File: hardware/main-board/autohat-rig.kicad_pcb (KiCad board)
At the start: 2 copper layers, 75.4 x 114 mm, 92 parts, among them J1 USDCARD, P1 USB HUB IN, P10 BARREL_JACK, P2 USB MUX 2, P3 USB MUX 1, P4 CONN_01X06, P5 BARREL_JACK, P6 IDC_02X04, P7 IDC_02X04, P8 PWR IN, P9 PWR OUT, Q1 IRF7606PBF, Q2 IRF7606PBF, Q3 IRF7606PBF, Q4 IRF7606PBF, Q5 2N7002, Q6 2N7002, Q7 IRF7606PBF, Q8 IRF7606PBF, U1 TS3USB30EDGSR, U2 FT245RL, U3 TUSB4041IPAPR, U4 74AHC1G14, U5 TLV73333, U6 TLV73311, U7 74AHC1G14, U8 TS3A27518E, Y1 24MHz

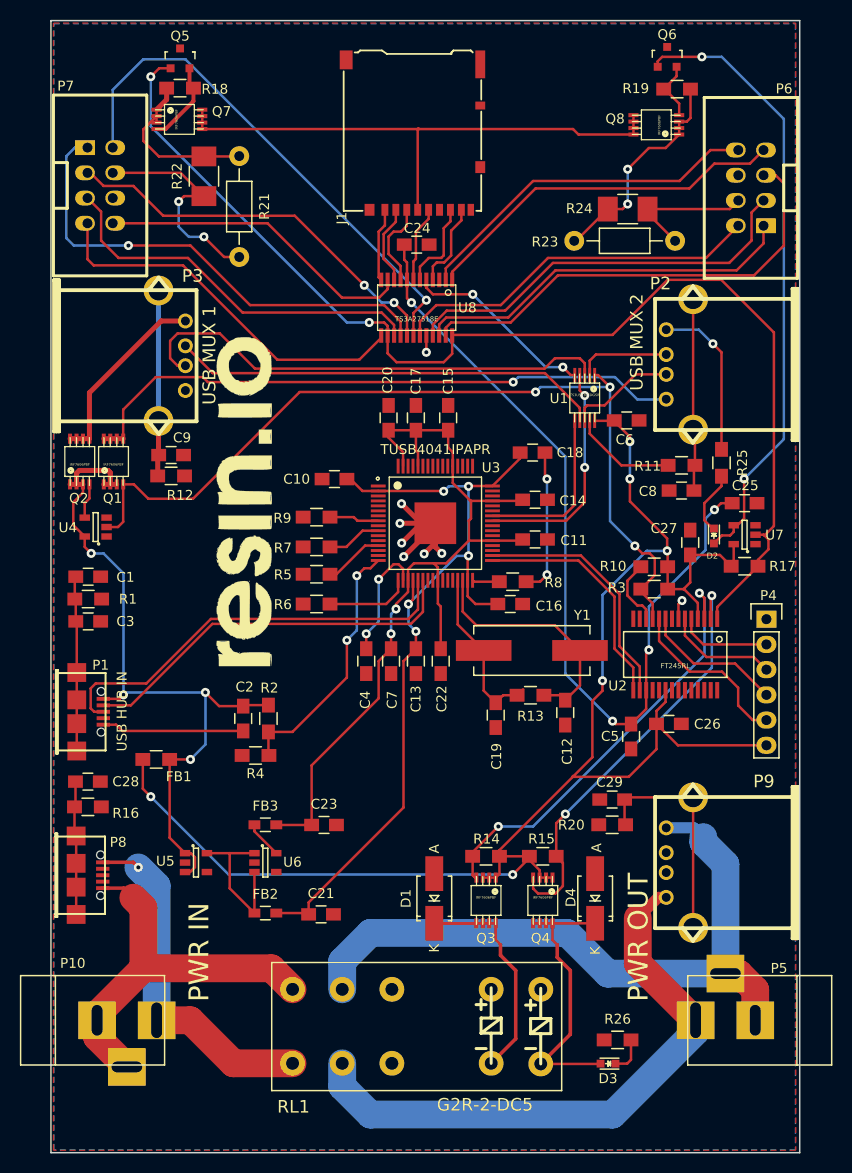
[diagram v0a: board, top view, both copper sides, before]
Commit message: Add mounting holes and labels
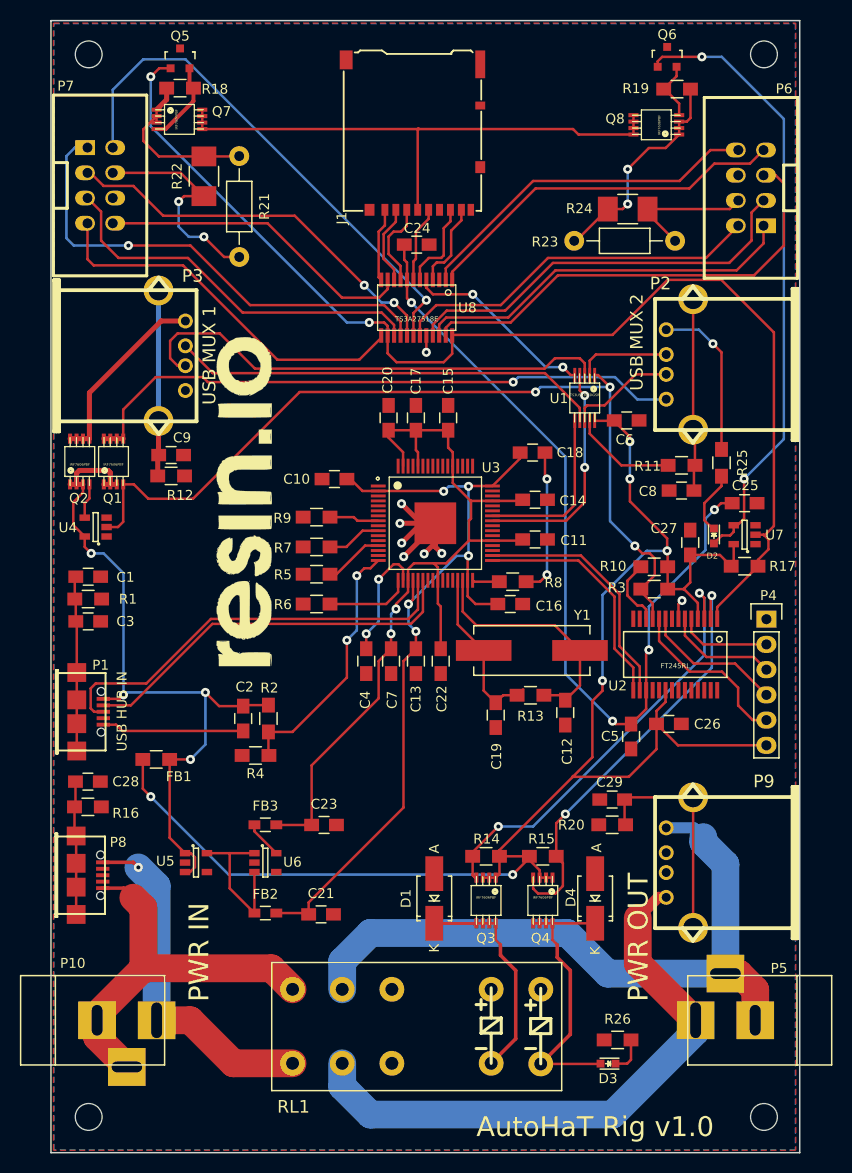
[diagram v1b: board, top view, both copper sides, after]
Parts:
- added REF**: MountingHole_2.7mm_M2.5, Mounting_Holes:MountingHole_2.7mm_M2.5, F.Cu at (122.0, 37.0)
- added REF**: MountingHole_2.7mm_M2.5, Mounting_Holes:MountingHole_2.7mm_M2.5, F.Cu at (190.0, 37.0)
- added REF**: MountingHole_2.7mm_M2.5, Mounting_Holes:MountingHole_2.7mm_M2.5, F.Cu at (122.0, 144.0)
- added REF**: MountingHole_2.7mm_M2.5, Mounting_Holes:MountingHole_2.7mm_M2.5, F.Cu at (190.0, 144.0)
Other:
- board text added: "AutoHaT Rig v1.0"
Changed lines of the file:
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@@
     (area 118.124519 33.525479 193.674521 147.675481)
     (thickness 1.6)
-    (drawings 7)
+    (drawings 9)
     (tracks 829)
     (zones 0)
-    (modules 92)
+    (modules 96)
     (nets 113)
   )
   (page A4)
   (title_block
-    (title sd-mux)
-    (date 2016-02-26)
-    (rev 2)
-    (company SRPOL)
-    (comment 1 "Author: Adam Malinowski <a.malinowsk2@partner.samsung.com>")
+    (title autohat-rig)
+    (date 2016-12-12)
+    (rev 1.0)
+    (company Resin.io)
+    (comment 1 "Author: Adam Malinowski <a.malinowsk2@partner.samsung.com> \\n        Tomás Villaseca <tomas@resin.io>")
     (comment 2 "Copyright (c) 2016 Samsung Electronics Co., Ltd All Rights Reserved")
   )
@@
     (zone_45_only yes)
     (trace_min 0.254)
-    (segment_width 0.2)
+    (segment_width 1)
     (edge_width 0.15)
     (via_size 0.91)
@@
     (pad_to_mask_clearance 0.2)
     (aux_axis_origin 118.19952 147.60048)
-    (visible_elements FFFEEF7F)
+    (visible_elements FFFEFF7F)
     (pcbplotparams
       (layerselection 0x010f0_80000001)
@@
     (add_net VDD)
   )
+  (module Mounting_Holes:MountingHole_2.7mm_M2.5 (layer Front)
+    (at 122 37)
+    (descr "Mounting Hole 2.7mm, no annular, M2.5")
+    (tags "mounting hole 2.7mm no annular m2.5")
+    (fp_text reference REF** (at 0 -3.7) (layer F.SilkS) hide
+      (effects (font (size 1 1) (thickness 0.15)))
+    )
+    (fp_text value MountingHole_2.7mm_M2.5 (at 0 3.7) (layer F.Fab)
+      (effects (font (size 1 1) (thickness 0.15)))
+    )
+    (fp_circle (center 0 0) (end 2.7 0) (layer Cmts.User) (width 0.15))
+    (fp_circle (center 0 0) (end 2.95 0) (layer F.CrtYd) (width 0.05))
+    (pad 1 np_thru_hole circle (at 0 0) (size 2.7 2.7) (drill 2.7) (layers *.Cu *.Mask))
+  )
+  (module Mounting_Holes:MountingHole_2.7mm_M2.5 (layer Front)
+    (at 190 37)
+    (descr "Mounting Hole 2.7mm, no annular, M2.5")
+    (tags "mounting hole 2.7mm no annular m2.5")
+    (fp_text reference REF** (at 0 -3.7) (layer F.SilkS) hide
+      (effects (font (size 1 1) (thickness 0.15)))
+    )
+    (fp_text value MountingHole_2.7mm_M2.5 (at 0 3.7) (layer F.Fab)
+      (effects (font (size 1 1) (thickness 0.15)))
+    )
+    (fp_circle (center 0 0) (end 2.7 0) (layer Cmts.User) (width 0.15))
+    (fp_circle (center 0 0) (end 2.95 0) (layer F.CrtYd) (width 0.05))
+    (pad 1 np_thru_hole circle (at 0 0) (size 2.7 2.7) (drill 2.7) (layers *.Cu *.Mask))
+  )
+  (module Mounting_Holes:MountingHole_2.7mm_M2.5 (layer Front)
+    (at 122 144)
+    (descr "Mounting Hole 2.7mm, no annular, M2.5")
+    (tags "mounting hole 2.7mm no annular m2.5")
+    (fp_text reference REF** (at 0 -3.7) (layer F.SilkS) hide
+      (effects (font (size 1 1) (thickness 0.15)))
+    )
+    (fp_text value MountingHole_2.7mm_M2.5 (at 0 3.7) (layer F.Fab)
+      (effects (font (size 1 1) (thickness 0.15)))
+    )
+    (fp_circle (center 0 0) (end 2.7 0) (layer Cmts.User) (width 0.15))
+    (fp_circle (center 0 0) (end 2.95 0) (layer F.CrtYd) (width 0.05))
+    (pad 1 np_thru_hole circle (at 0 0) (size 2.7 2.7) (drill 2.7) (layers *.Cu *.Mask))
+  )
   (module TO_SOT_Packages_SMD:SOT-23-5 (layer Front)
     (at 188.04952 85.37048 180)
@@
       (effects (font (thickness 0.3048)))
     )
-    (fp_text value G2R-2-DC5 (at -6.87008 -7.87292 180) (layer F.SilkS)
+    (fp_text value G2R-2-DC5 (at -6.87008 -7.87292 180) (layer F.SilkS) hide
       (effects (font (thickness 0.3048)))
     )
@@
       (effects (font (size 1 1) (thickness 0.15)))
     )
-    (fp_text value TUSB4041IPAPR (at 0.01168 -7.43128) (layer F.SilkS)
+    (fp_text value TUSB4041IPAPR (at 0.01168 -7.43128) (layer F.SilkS) hide
       (effects (font (size 1 1) (thickness 0.05)))
     )
@@
       (xy 12.361334 0.889)) (layer F.SilkS) (width 0.01))
   )
+  (module Mounting_Holes:MountingHole_2.7mm_M2.5 (layer Front)
+    (at 190 144)
+    (descr "Mounting Hole 2.7mm, no annular, M2.5")
+    (tags "mounting hole 2.7mm no annular m2.5")
+    (fp_text reference REF** (at 0 -3.7) (layer F.SilkS) hide
+      (effects (font (size 1 1) (thickness 0.15)))
+    )
+    (fp_text value MountingHole_2.7mm_M2.5 (at 0 3.7) (layer F.Fab)
+      (effects (font (size 1 1) (thickness 0.15)))
+    )
+    (fp_circle (center 0 0) (end 2.7 0) (layer Cmts.User) (width 0.15))
+    (fp_circle (center 0 0) (end 2.95 0) (layer F.CrtYd) (width 0.05))
+    (pad 1 np_thru_hole circle (at 0 0) (size 2.7 2.7) (drill 2.7) (layers *.Cu *.Mask))
+  )
+  (gr_line (start 181 41) (end 151 41) (angle 90) (layer B.SilkS) (width 10))
+  (target plus (at 145.75 144.75) (size 5) (width 0.15) (layer Edge.Cuts))
+  (gr_text "AutoHaT Rig v1.0" (at 173 145) (layer F.SilkS)
+    (effects (font (size 2 2) (thickness 0.5)))
+  )
   (dimension 75.3 (width 0.3) (layer Dwgs.User)
     (gr_text "75.300 mm" (at 155.74952 153.85048) (layer Dwgs.User)
@@
     (arrow2b (pts (xy 112.79952 33.60048) (xy 113.385941 34.726984)))
   )
-  (target plus (at 145.75 144.75) (size 5) (width 0.15) (layer Edge.Cuts))
   (gr_line (start 193.59952 147.60048) (end 118.19952 147.60048) (angle 90) (layer Edge.Cuts) (width 0.15))
   (gr_line (start 193.59952 33.60048) (end 193.59952 147.60048) (angle 90) (layer Edge.Cuts) (width 0.15))

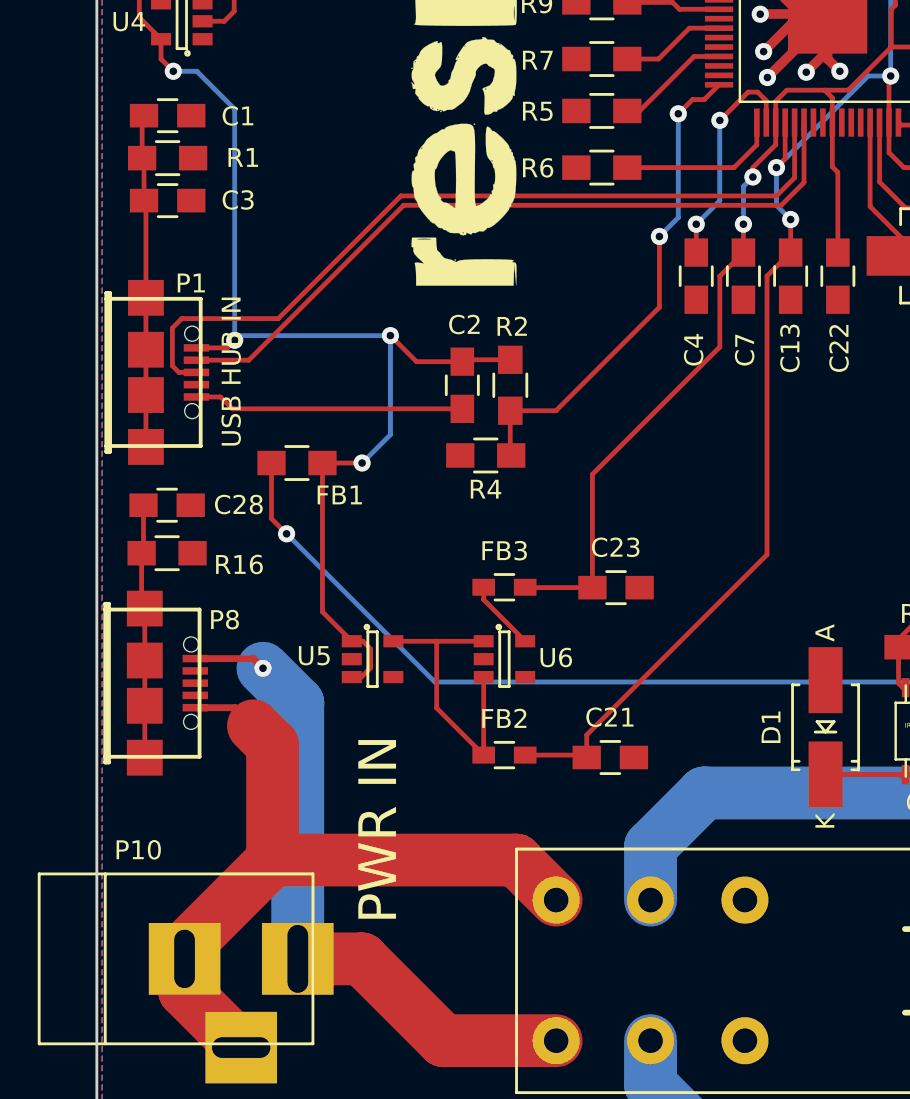
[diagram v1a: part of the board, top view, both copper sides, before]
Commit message: Change micro USB socket to through-hole
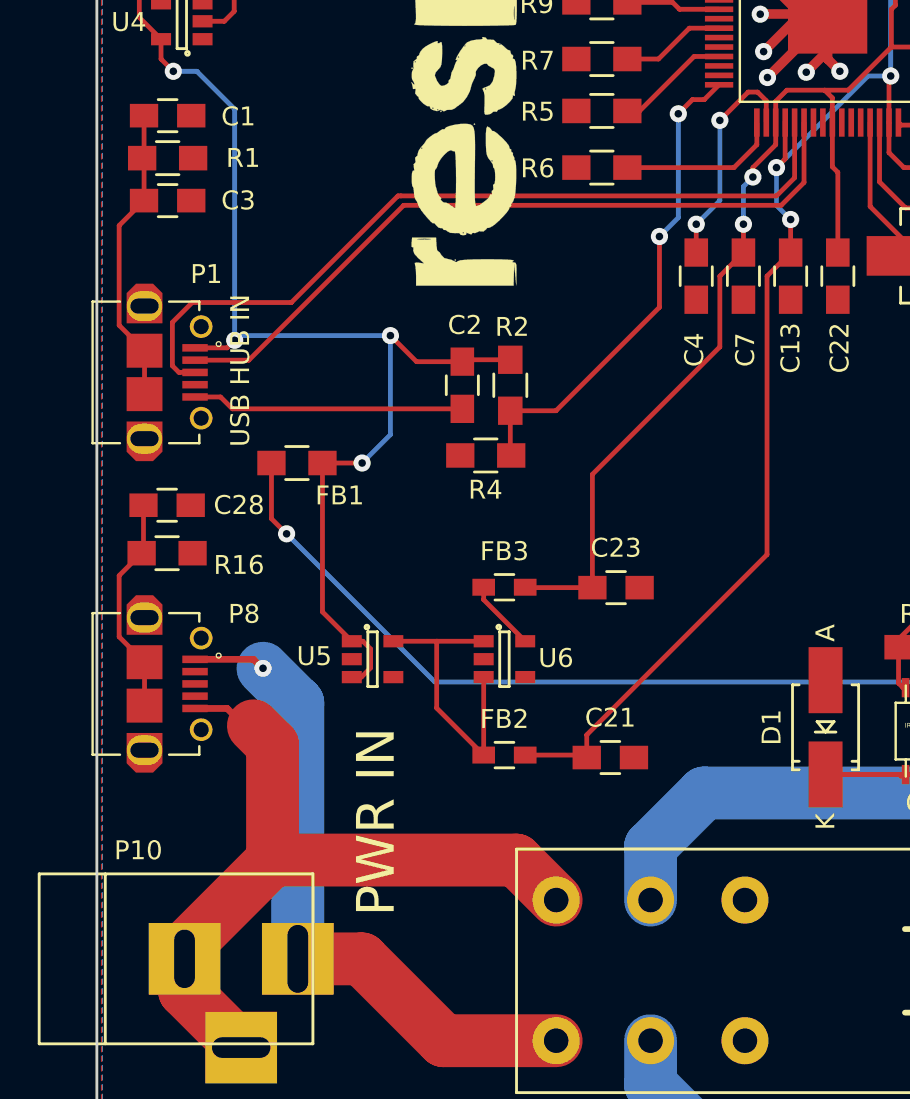
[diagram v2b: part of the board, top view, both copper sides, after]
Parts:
- P1, P8: footprint footprints:conn_usb_B_micro -> footprints:TO_microUSB
- RL1: value G2R-2-DC5 -> G2RK-2-DC5
- moved P8 2.66 mm to (123.4, 119.7)
- moved P1 2.60 mm to (123.4, 103.2)
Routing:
- net Net-(C1-Pad1): track 17.7 -> 15.9 mm
- net Net-(C28-Pad1): track 13.5 -> 11.7 mm

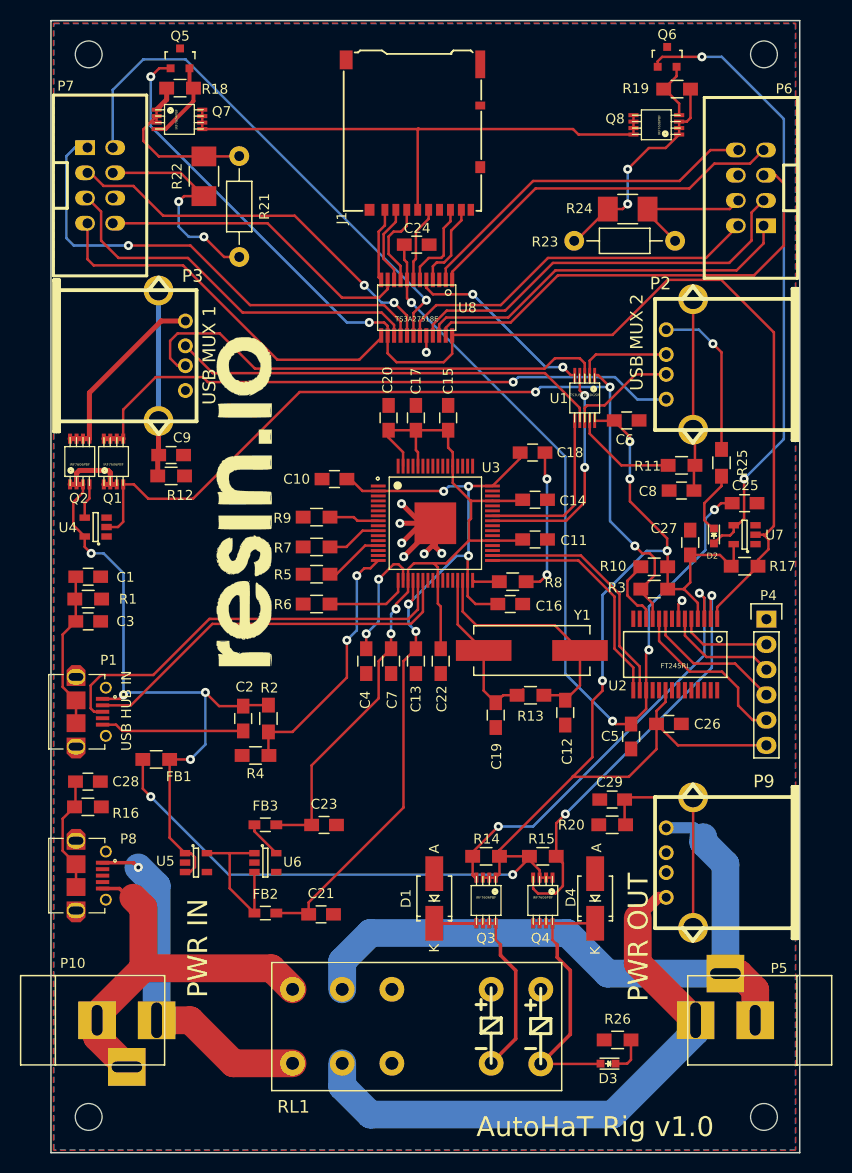
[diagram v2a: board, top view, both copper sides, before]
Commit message: Fix current leakage
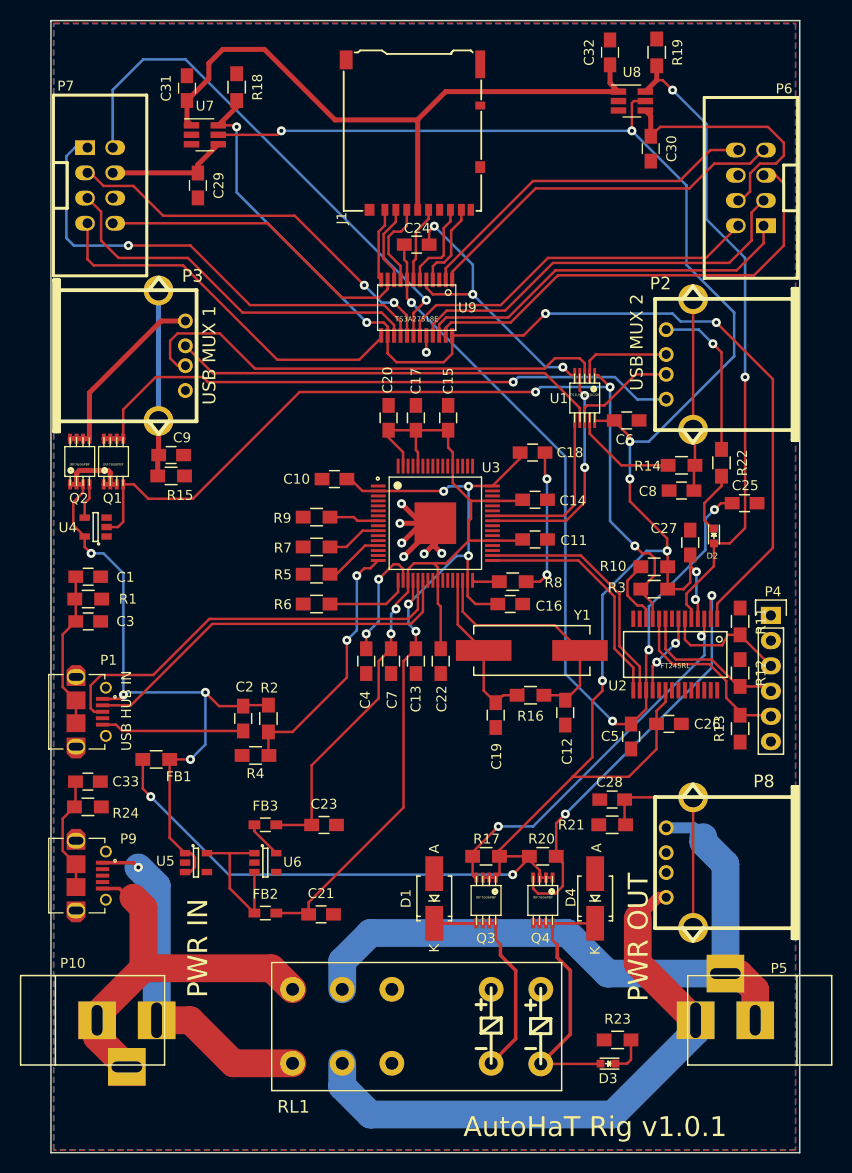
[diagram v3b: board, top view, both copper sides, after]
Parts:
- removed G***: LOGO, footprints:logo
- removed Q5, Q6: 2N7002, TO_SOT_Packages_SMD:SOT-23
- removed Q7, Q8: IRF7606PBF, footprints:msoic-8
- removed the R17 at (188.0, 88.5)
- removed the R21 at (137.2, 57.4)
- removed the R22 at (133.6, 49.3)
- removed the R23 at (181.1, 55.8)
- removed the R24 at (176.3, 52.6)
- removed REF** (x4): MountingHole_2.7mm_M2.5, Mounting_Holes:MountingHole_2.7mm_M2.5
- added C29: 1u, Capacitors_SMD:C_0805_HandSoldering, F.Cu at (133.0, 50.2)
- added C30: 1u, Capacitors_SMD:C_0805_HandSoldering, F.Cu at (178.6, 46.5)
- added C31: 100n, Capacitors_SMD:C_0805_HandSoldering, F.Cu at (131.9, 40.4)
- added C32: 100n, Capacitors_SMD:C_0805_HandSoldering, F.Cu at (174.5, 36.8)
- added R11: 10K, Resistors_SMD:R_0805_HandSoldering, F.Cu at (187.6, 94.1)
- added R12: 10K, Resistors_SMD:R_0805_HandSoldering, F.Cu at (187.6, 99.3)
- added R13: 10K, Resistors_SMD:R_0805_HandSoldering, F.Cu at (187.6, 104.9)
- added U8: TPS22860, TO_SOT_Packages_SMD:SOT-23-6_Handsoldering, F.Cu at (176.7, 41.7)
- U7: value 74AHC1G14 -> TPS22860; footprint TO_SOT_Packages_SMD:SOT-23-5 -> TO_SOT_Packages_SMD:SOT-23-6_Handsoldering
- moved U7 67.6 mm to (133.7, 45.1), turned to 0 degrees
- moved R18 5.70 mm to (136.9, 40.3), turned to 270 degrees
- moved R19 4.23 mm to (179.2, 36.8), turned to 270 degrees
- moved P4 0.59 mm to (190.7, 93.5)
- renumbered C29 to C28, C28 to C33, P9 to P8, P8 to P9, R11 to R14, R12 to R15, R13 to R16, R14 to R17, R15 to R20, R20 to R21, R25 to R22, R26 to R23, R16 to R24, U8 to U9
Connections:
- D2 pad 2: Net-(D2-Pad2) -> /DUT_SEL
- R18 pad 1: Net-(Q7-Pad1) -> GND
- R18 pad 2: Net-(Q5-Pad2) -> /TS_SEL
- R19 pad 1: Net-(Q8-Pad1) -> GND
- R19 pad 2: Net-(Q6-Pad2) -> /DUT_SEL
- U2 pad 1: /SOCKET_SEL -> /TS_SEL
- U2 pad 5: Net-(P4-Pad2) -> /DUT_SEL
- U7 pad 1: (no net) -> /USD_VDD
- U7 pad 2: /SOCKET_SEL -> GND
- U7 pad 3: GND -> (no net)
- U7 pad 4: Net-(D2-Pad2) -> /VDD_TS
- U9 pad 14: /SOCKET_SEL -> /TS_SEL
- U9 pad 24: /SOCKET_SEL -> /TS_SEL
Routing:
- net /SOCKET_SEL: track 120.7 -> 0.00 mm, vias 2 -> 0
- net /TS_SEL: track 0.00 -> 106.8 mm, vias 0 -> 4
- net VDD: track 160.7 -> 232.2 mm, vias 6 -> 10
- net /DUT_SEL: track 0.00 -> 64.9 mm, vias 0 -> 2
- net Net-(D2-Pad2): track 62.4 -> 0.00 mm, vias 2 -> 0
- net Net-(Q8-Pad1): track 22.8 -> 0.00 mm, vias 2 -> 0
- net Net-(Q7-Pad1): track 17.2 -> 0.00 mm
- net GND: track 102.5 -> 119.4 mm, vias 13 -> 15
- net /VDD_DUT: track 14.1 -> 26.1 mm
- net /VDD_TS: track 22.8 -> 12.4 mm, vias 2 -> 0
- net /USD_VDD: track 55.8 -> 65.4 mm
- net Net-(P4-Pad2): track 9.43 -> 0.00 mm
- net Net-(Q5-Pad2): track 8.36 -> 0.00 mm
- net Net-(Q6-Pad2): track 6.11 -> 0.00 mm
- net /POWER_SW_OFF: track 43.6 -> 38.3 mm
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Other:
- board text added: "AutoHaT Rig v1.0.1"
- board text removed: "AutoHaT Rig v1.0"
